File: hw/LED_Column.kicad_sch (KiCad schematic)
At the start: 0 parts

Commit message: added LED Matrix sch
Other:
- added sheet RGB LED Cell 1 (RGB_LED_Cell.kicad_sch)
- added sheet RGB LED Cell 2 (RGB_LED_Cell.kicad_sch)
- added sheet RGB LED Cell 3 (RGB_LED_Cell.kicad_sch)
- added sheet RGB LED Cell 4 (RGB_LED_Cell.kicad_sch)
- added sheet RGB LED Cell 5 (RGB_LED_Cell.kicad_sch)
- added sheet RGB LED Cell 6 (RGB_LED_Cell.kicad_sch)
- added sheet RGB LED Cell 7 (RGB_LED_Cell.kicad_sch)
- added sheet RGB LED Cell 8 (RGB_LED_Cell.kicad_sch)

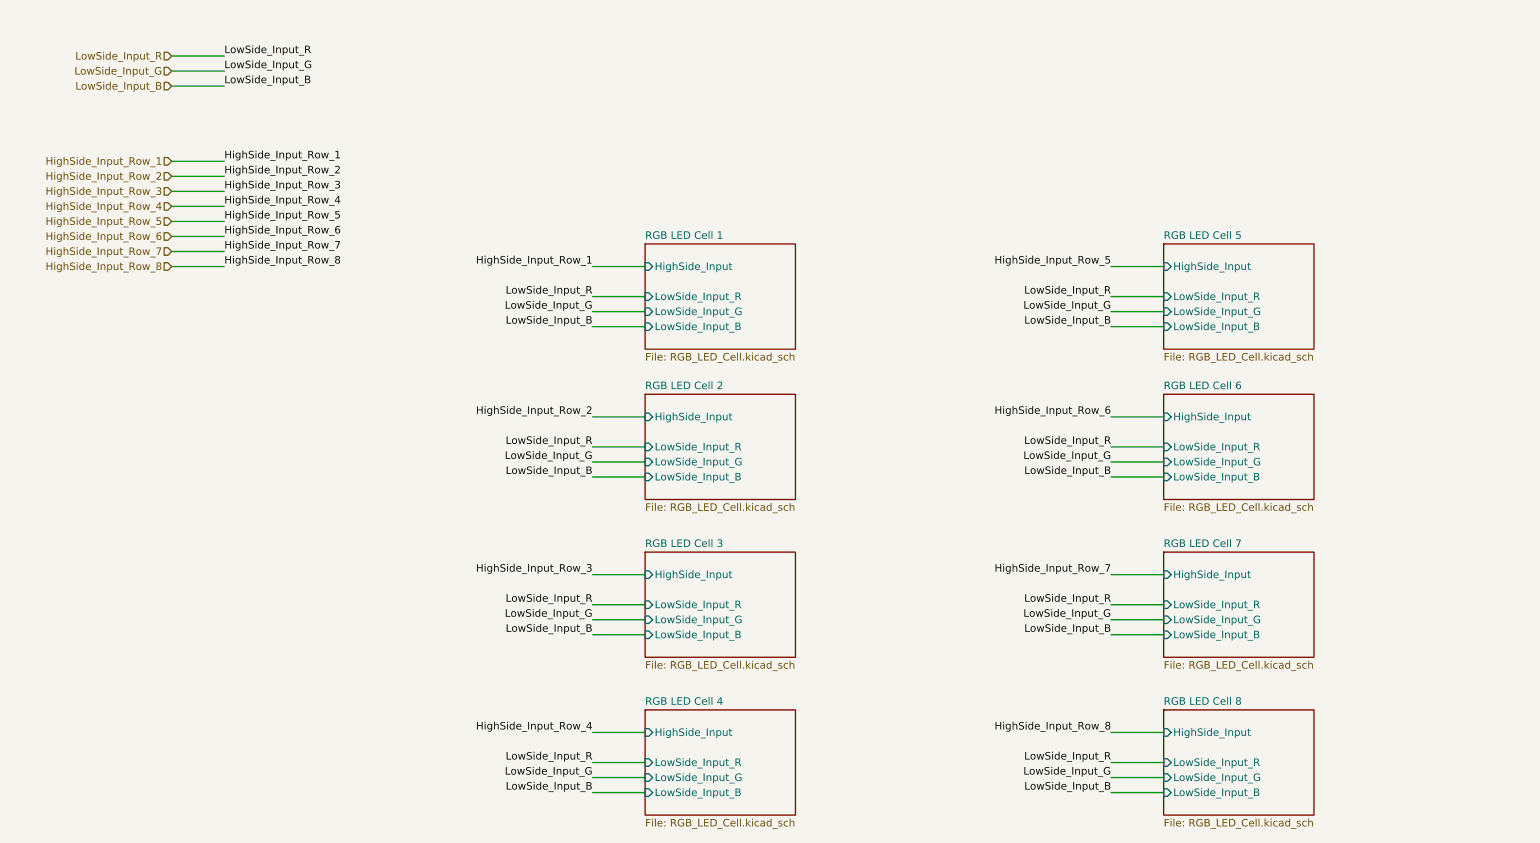
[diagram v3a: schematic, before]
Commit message: added NMOS matrix
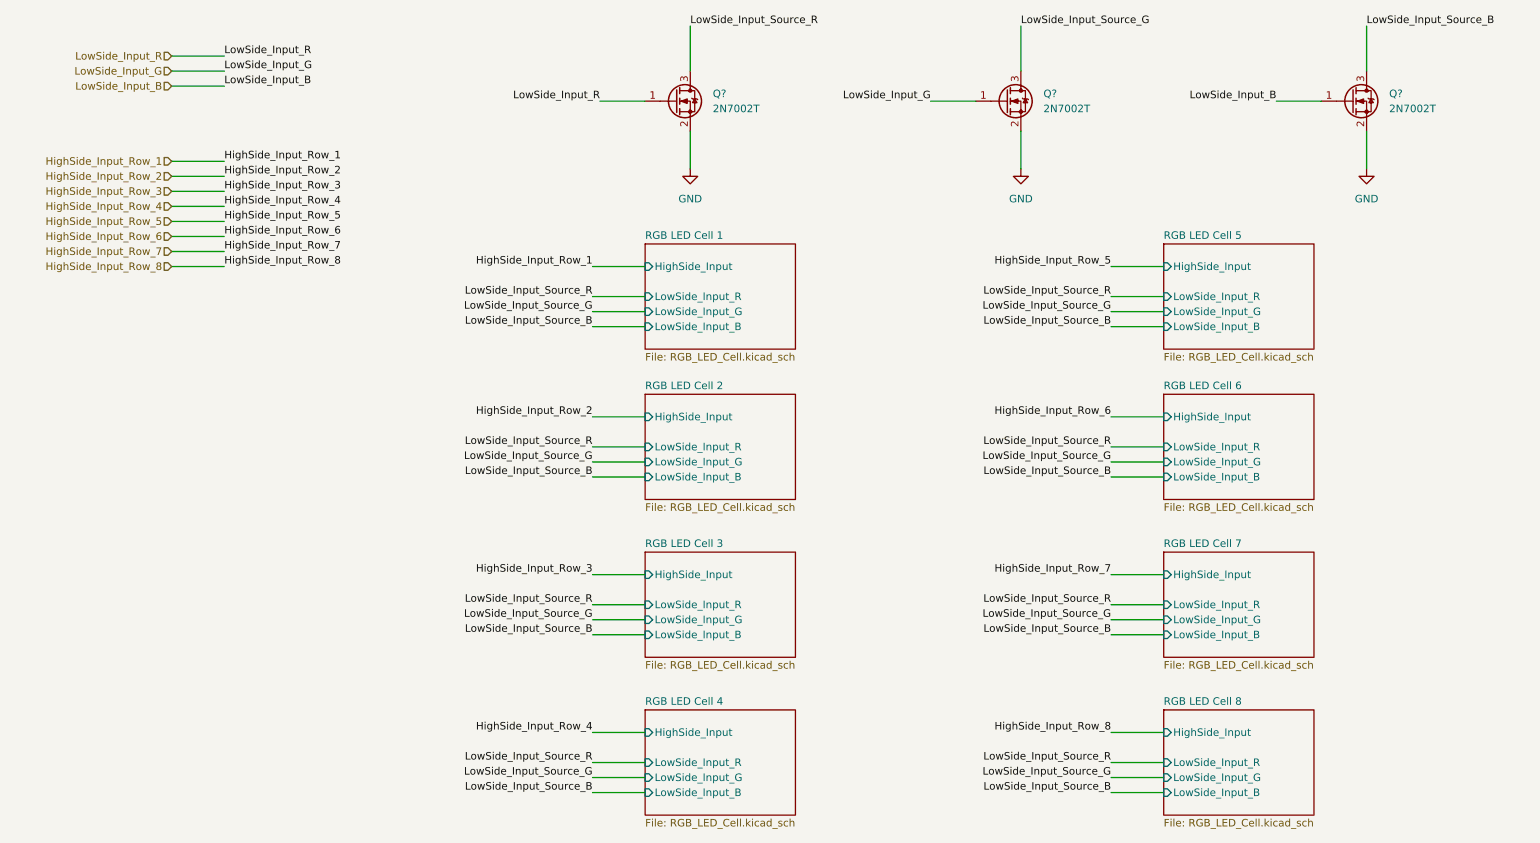
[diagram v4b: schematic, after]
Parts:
- added Q? (x3): 2N7002T, Package_TO_SOT_SMD:SOT-523, symbol Device:Q_NMOS_GSD
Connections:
- net LowSide_Input_B: now also Q?.1 (G)
- net LowSide_Input_G: now also Q?.1 (G)
- net LowSide_Input_R: now also Q?.1 (G)
- new net GND: Q?.2 (S), Q?.2 (S), Q?.2 (S)
- new net LowSide_Input_Source_B: Q?.3 (D)
- new net LowSide_Input_Source_G: Q?.3 (D)
- new net LowSide_Input_Source_R: Q?.3 (D)

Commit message: updated sheets information
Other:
- company: (none) -> Qingdao IotPi Information Technology Ltd.,
- title: (none) -> KiCad 2023 Shen Zhen Badge
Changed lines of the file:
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@@
 (kicad_sch (version 20230121) (generator eeschema)
   (paper "A4")
+  (title_block
+    (title "KiCad 2023 Shen Zhen Badge")
+    (date "2023-09-04")
+    (rev "1")
+    (company "Qingdao IotPi Information Technology Ltd.,")
+    (comment 1 "Designed by Yang Hongbo")
+  )
   (wire (pts (xy 241.3 43.18) (xy 241.3 36.83))
     (stroke (width 0) (type default))

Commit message: updated components LCSC (2N7002T)
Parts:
- Q? (x3): LCSC (none) -> C5224243; Vendor (none) -> ElecSuper(静芯微）; Vendor Model (none) -> 2N7002T
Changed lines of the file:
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@@
+      (effects (font (size 1.27 1.27)) hide)
+    )
+    (property "Description" "类型: N沟道 漏源电压(Vdss): 60V 连续漏极电流(Id): 300mA 功率(Pd): 200mW 导通电阻(RDS(on)@Vgs,Id):" (at 180.34 31.75 0)
+      (effects (font (size 1.27 1.27)) hide)
+    )
+    (property "LCSC" "C5224243" (at 180.34 31.75 0)
+      (effects (font (size 1.27 1.27)) hide)
+    )
+    (property "Vendor" "ElecSuper(静芯微）" (at 180.34 31.75 0)
+      (effects (font (size 1.27 1.27)) hide)
+    )
+    (property "Vendor Model" "2N7002T" (at 180.34 31.75 0)
       (effects (font (size 1.27 1.27)) hide)
     )
@@
       (effects (font (size 1.27 1.27)) hide)
     )
+    (property "Description" "类型: N沟道 漏源电压(Vdss): 60V 连续漏极电流(Id): 300mA 功率(Pd): 200mW 导通电阻(RDS(on)@Vgs,Id):" (at 238.76 31.75 0)
+      (effects (font (size 1.27 1.27)) hide)
+    )
+    (property "LCSC" "C5224243" (at 238.76 31.75 0)
+      (effects (font (size 1.27 1.27)) hide)
+    )
+    (property "Vendor" "ElecSuper(静芯微）" (at 238.76 31.75 0)
+      (effects (font (size 1.27 1.27)) hide)
+    )
+    (property "Vendor Model" "2N7002T" (at 238.76 31.75 0)
+      (effects (font (size 1.27 1.27)) hide)
+    )
     (pin "1")
     (pin "2")
@@
       (effects (font (size 1.27 1.27)) hide)
     )
+    (property "Description" "类型: N沟道 漏源电压(Vdss): 60V 连续漏极电流(Id): 300mA 功率(Pd): 200mW 导通电阻(RDS(on)@Vgs,Id):" (at 124.46 31.75 0)
+      (effects (font (size 1.27 1.27)) hide)
+    )
+    (property "LCSC" "C5224243" (at 124.46 31.75 0)
+      (effects (font (size 1.27 1.27)) hide)
+    )
+    (property "Vendor" "ElecSuper(静芯微）" (at 124.46 31.75 0)
+      (effects (font (size 1.27 1.27)) hide)
+    )
+    (property "Vendor Model" "2N7002T" (at 124.46 31.75 0)
+      (effects (font (size 1.27 1.27)) hide)
+    )
